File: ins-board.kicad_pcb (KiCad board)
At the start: 2 copper layers, 47 parts, among them P1 CONN_8, P2 PWR, U1 STM32F042C6T6, U2 MIC5201-3.3YS, U3 H3LIS331DL, U4 MPU6000, U5 MS5611-01BA, X1 CRYSTAL 16MHz 10ppm

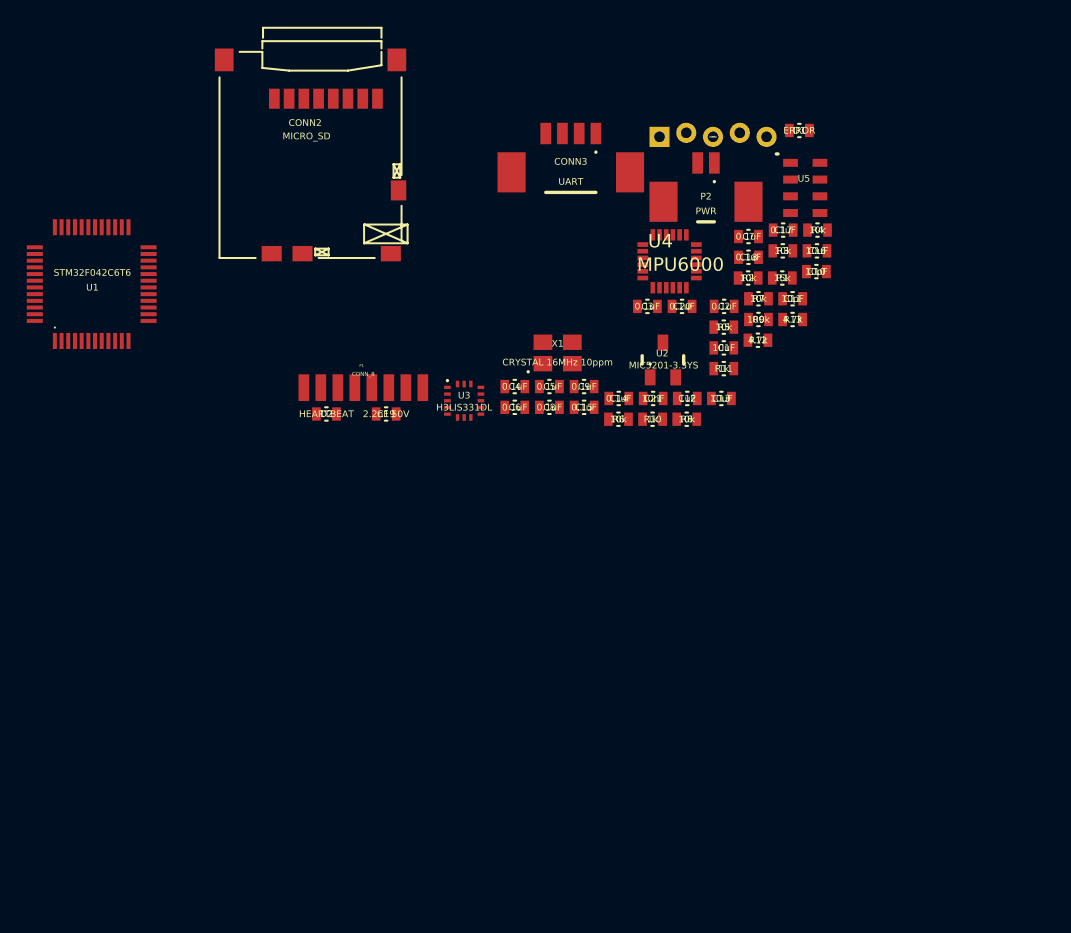
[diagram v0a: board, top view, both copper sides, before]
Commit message: Component placement on PCB
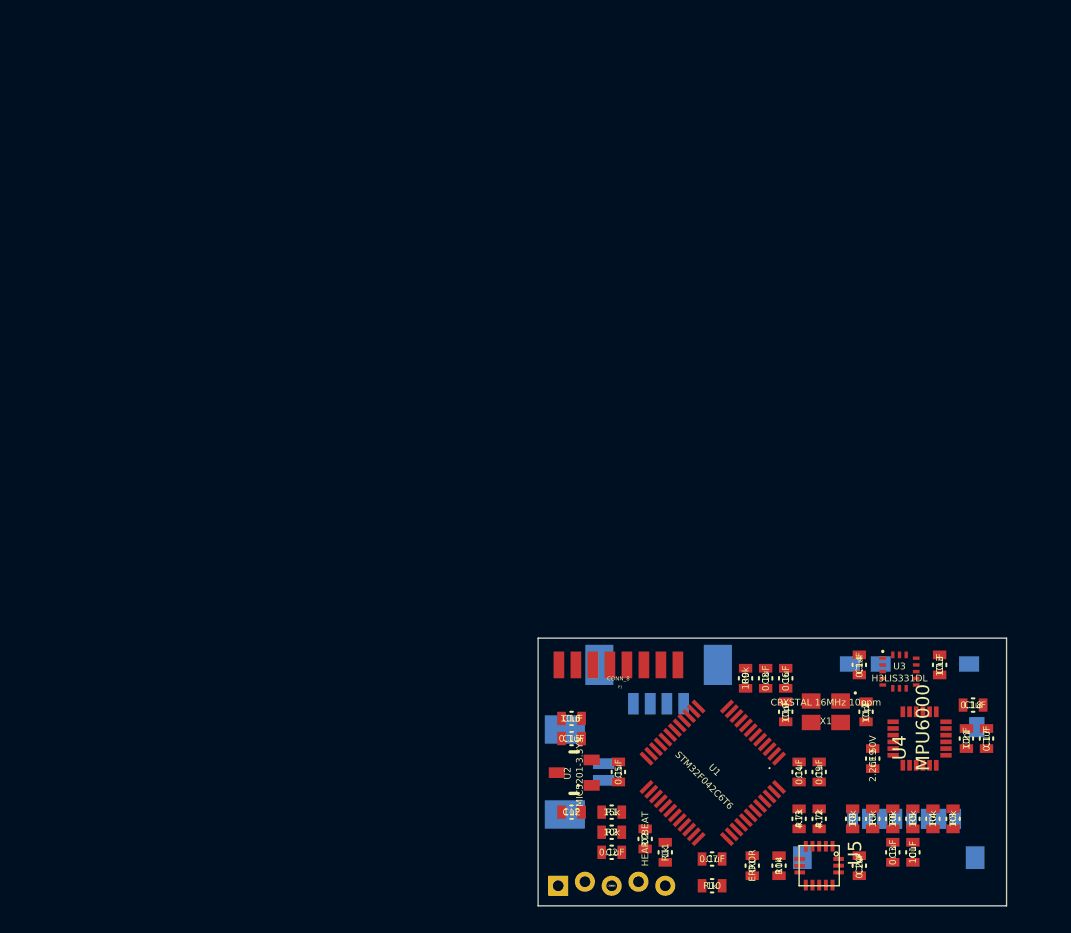
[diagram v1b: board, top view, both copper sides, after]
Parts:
- added R14: 10k, _std:_0603-W, F.Cu at (151.0, 104.5)
- CONN2, CONN3, P2: moved to B.Cu
- U5: value MS5611-01BA -> LPS331AP; footprint _sensors:_MS5611-01BA -> _sensors:_LPS331AP
- moved CONN2 69.0 mm to (156.5, 101.0)
- moved U1 62.5 mm to (151.0, 96.5), turned to 135 degrees
- moved CONN1 56.5 mm to (138.5, 106.0)
- moved D1 55.0 mm to (149.0, 104.5), turned to 270 degrees
- moved U5 49.2 mm to (155.5, 103.0), turned to 270 degrees
- moved C7 46.6 mm to (146.0, 104.0), turned to 180 degrees
- moved R4 44.8 mm to (162.5, 101.0), turned to 90 degrees
- moved C3 44.7 mm to (159.5, 103.5), turned to 270 degrees
- moved C19 44.5 mm to (158.0, 96.5), turned to 90 degrees
- moved R3 44.3 mm to (164.0, 101.0), turned to 90 degrees
- moved P2 43.9 mm to (135.0, 97.5), turned to 90 degrees
- moved C20 43.8 mm to (157.0, 104.5), turned to 270 degrees
- moved R2 42.6 mm to (138.5, 102.0)
- moved R1 41.9 mm to (138.5, 100.5), turned to 180 degrees
- moved C2 41.6 mm to (138.5, 103.5)
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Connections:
- U1 pad 10: (no net) -> Net-(U1-Pad10)
- U1 pad 18: (no net) -> Net-(U1-Pad18)
- U1 pad 2: (no net) -> Net-(U1-Pad2)
- U1 pad 21: (no net) -> Net-(U1-Pad21)
- U1 pad 22: (no net) -> Net-(U1-Pad22)
- U1 pad 3: (no net) -> Net-(U1-Pad3)
- U1 pad 32: (no net) -> Net-(U1-Pad32)
- U1 pad 33: (no net) -> Net-(U1-Pad33)
- U1 pad 4: (no net) -> Net-(U1-Pad4)
- U1 pad 40: (no net) -> Net-(U1-Pad40)
- U1 pad 41: (no net) -> Net-(U1-Pad41)
- U1 pad 45: (no net) -> Net-(U1-Pad45)
- U1 pad 46: (no net) -> Net-(U1-Pad46)
- U3 pad 9: (no net) -> Net-(U3-Pad9)
- U4 pad 22: (no net) -> Net-(U4-Pad22)
- U4 pad 6: (no net) -> Net-(U4-Pad6)
- U4 pad 7: (no net) -> Net-(U4-Pad7)
- U5 pad 2: VCC -> Net-(U5-Pad2)
- U5 pad 3: GND -> Net-(U5-Pad3)
- U5 pad 4: GND -> /INT_I2C_SCL
- U5 pad 6: (no net) -> /INT_I2C_SDA
- U5 pad 7: /INT_I2C_SDA -> GND
- U5 pad 8: /INT_I2C_SCL -> Net-(R14-Pad2)
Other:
- board outline added: 35 x 20 mm

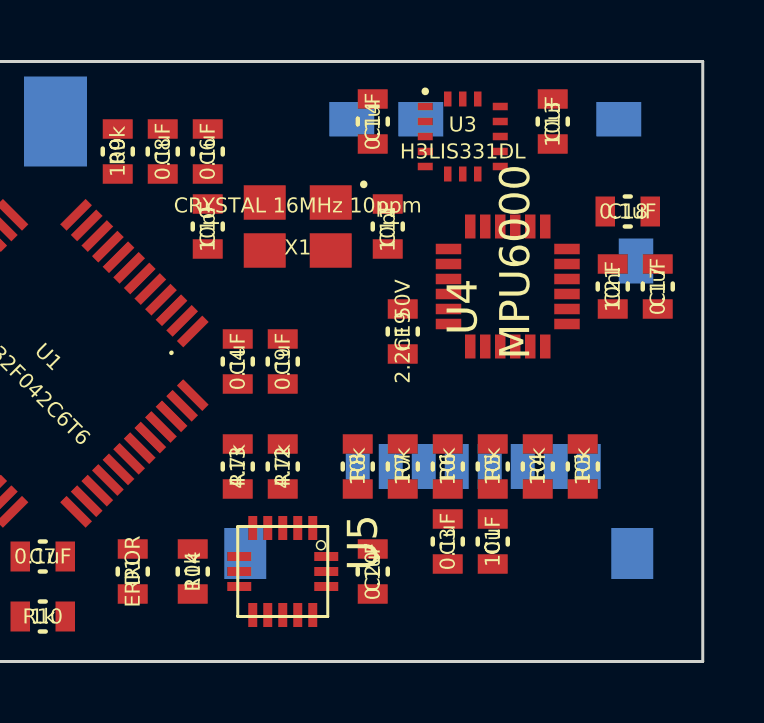
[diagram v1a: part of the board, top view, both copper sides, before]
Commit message: Correct microSD connector footprint & update component placement
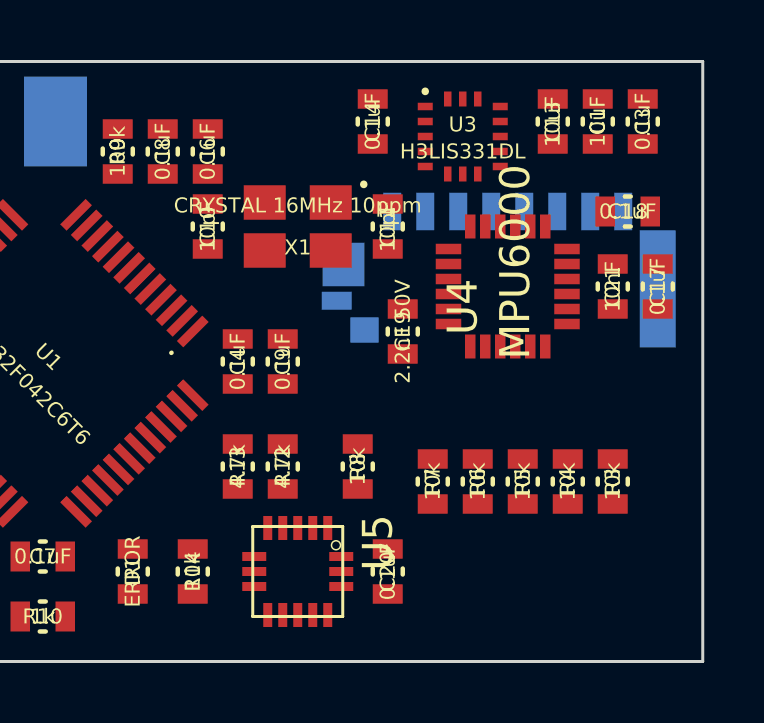
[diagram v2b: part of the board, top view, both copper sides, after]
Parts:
- CONN2: footprint _div:_Molex-microSD-502570-0893 -> _div:_Molex-microSD-WM6701
- moved C3 15.4 mm to (166.0, 89.5)
- moved C1 14.4 mm to (164.5, 89.5)
- moved CONN2 9.86 mm to (161.5, 92.5), turned to 180 degrees
- moved R3 1.12 mm to (165.0, 101.5), turned to 270 degrees
- moved R4 1.12 mm to (163.5, 101.5), turned to 270 degrees
- moved R5 1.12 mm to (162.0, 101.5), turned to 270 degrees
- moved R6 1.12 mm to (160.5, 101.5), turned to 270 degrees
- moved R7 1.12 mm to (159.0, 101.5), turned to 270 degrees
- moved C20 0.50 mm to (157.5, 104.5)
- moved U5 0.50 mm to (156.0, 103.0)

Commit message: update sd-card footprint
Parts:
- moved CONN2 1.10 mm to (161.4, 91.4)
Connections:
- U1 pad 10: Net-(U1-Pad10) -> (no net)
- U1 pad 18: Net-(U1-Pad18) -> (no net)
- U1 pad 2: Net-(U1-Pad2) -> (no net)
- U1 pad 21: Net-(U1-Pad21) -> (no net)
- U1 pad 22: Net-(U1-Pad22) -> (no net)
- U1 pad 3: Net-(U1-Pad3) -> (no net)
- U1 pad 32: Net-(U1-Pad32) -> (no net)
- U1 pad 33: Net-(U1-Pad33) -> (no net)
- U1 pad 4: Net-(U1-Pad4) -> (no net)
- U1 pad 40: Net-(U1-Pad40) -> (no net)
- U1 pad 41: Net-(U1-Pad41) -> (no net)
- U1 pad 45: Net-(U1-Pad45) -> (no net)
- U1 pad 46: Net-(U1-Pad46) -> (no net)
- U3 pad 9: Net-(U3-Pad9) -> (no net)
- U4 pad 22: Net-(U4-Pad22) -> (no net)
- U4 pad 6: Net-(U4-Pad6) -> (no net)
- U4 pad 7: Net-(U4-Pad7) -> (no net)
- U5 pad 11: Net-(U5-Pad11) -> (no net)
- U5 pad 2: Net-(U5-Pad2) -> (no net)
- U5 pad 3: Net-(U5-Pad3) -> (no net)
- U5 pad 9: Net-(U5-Pad9) -> (no net)
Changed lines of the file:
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@@
-(kicad_pcb (version 4) (host pcbnew "(2015-03-28 BZR 5545)-product")
+(kicad_pcb (version 4) (host pcbnew "(2015-03-28 BZR 5547)-product")
   (general
     (links 152)
@@
     (zones 0)
     (modules 48)
-    (nets 57)
+    (nets 36)
   )
   (page A4)
@@
   (net 34 /MPU6000_INT)
   (net 35 "Net-(R14-Pad2)")
-  (net 36 "Net-(U1-Pad2)")
-  (net 37 "Net-(U1-Pad3)")
-  (net 38 "Net-(U1-Pad4)")
-  (net 39 "Net-(U1-Pad10)")
-  (net 40 "Net-(U1-Pad18)")
-  (net 41 "Net-(U1-Pad21)")
-  (net 42 "Net-(U1-Pad22)")
-  (net 43 "Net-(U1-Pad32)")
-  (net 44 "Net-(U1-Pad33)")
-  (net 45 "Net-(U1-Pad40)")
-  (net 46 "Net-(U1-Pad41)")
-  (net 47 "Net-(U1-Pad45)")
-  (net 48 "Net-(U1-Pad46)")
-  (net 49 "Net-(U3-Pad9)")
-  (net 50 "Net-(U4-Pad22)")
-  (net 51 "Net-(U4-Pad7)")
-  (net 52 "Net-(U4-Pad6)")
-  (net 53 "Net-(U5-Pad2)")
-  (net 54 "Net-(U5-Pad3)")
-  (net 55 "Net-(U5-Pad9)")
-  (net 56 "Net-(U5-Pad11)")
   (net_class Default "This is the default net class."
     (clearance 0.2)
@@
     (add_net "Net-(P1-Pad8)")
     (add_net "Net-(R14-Pad2)")
-    (add_net "Net-(U1-Pad10)")
-    (add_net "Net-(U1-Pad18)")
-    (add_net "Net-(U1-Pad2)")
-    (add_net "Net-(U1-Pad21)")
-    (add_net "Net-(U1-Pad22)")
-    (add_net "Net-(U1-Pad3)")
-    (add_net "Net-(U1-Pad32)")
-    (add_net "Net-(U1-Pad33)")
-    (add_net "Net-(U1-Pad4)")
-    (add_net "Net-(U1-Pad40)")
-    (add_net "Net-(U1-Pad41)")
-    (add_net "Net-(U1-Pad45)")
-    (add_net "Net-(U1-Pad46)")
-    (add_net "Net-(U3-Pad9)")
-    (add_net "Net-(U4-Pad22)")
-    (add_net "Net-(U4-Pad6)")
-    (add_net "Net-(U4-Pad7)")
-    (add_net "Net-(U5-Pad11)")
-    (add_net "Net-(U5-Pad2)")
-    (add_net "Net-(U5-Pad3)")
-    (add_net "Net-(U5-Pad9)")
     (add_net VCC)
   )
@@
     (pad 1 smd rect (at 0 0 135) (size 0.3 1.2) (layers F.Cu F.Paste F.Mask)
       (net 2 VCC))
-    (pad 2 smd rect (at 0.5 0 135) (size 0.3 1.2) (layers F.Cu F.Paste F.Mask)
-      (net 36 "Net-(U1-Pad2)"))
-    (pad 3 smd rect (at 1 0 135) (size 0.3 1.2) (layers F.Cu F.Paste F.Mask)
-      (net 37 "Net-(U1-Pad3)"))
-    (pad 4 smd rect (at 1.5 0 135) (size 0.3 1.2) (layers F.Cu F.Paste F.Mask)
-      (net 38 "Net-(U1-Pad4)"))
+    (pad 2 smd rect (at 0.5 0 135) (size 0.3 1.2) (layers F.Cu F.Paste F.Mask))
+    (pad 3 smd rect (at 1 0 135) (size 0.3 1.2) (layers F.Cu F.Paste F.Mask))
+    (pad 4 smd rect (at 1.5 0 135) (size 0.3 1.2) (layers F.Cu F.Paste F.Mask))
     (pad 5 smd rect (at 2 0 135) (size 0.3 1.2) (layers F.Cu F.Paste F.Mask)
       (net 5 "Net-(C10-Pad1)"))
@@
     (pad 9 smd rect (at 4 0 135) (size 0.3 1.2) (layers F.Cu F.Paste F.Mask)
       (net 2 VCC))
-    (pad 10 smd rect (at 4.5 0 135) (size 0.3 1.2) (layers F.Cu F.Paste F.Mask)
-      (net 39 "Net-(U1-Pad10)"))
+    (pad 10 smd rect (at 4.5 0 135) (size 0.3 1.2) (layers F.Cu F.Paste F.Mask))
     (pad 11 smd rect (at 5 0 135) (size 0.3 1.2) (layers F.Cu F.Paste F.Mask)
       (net 3 /V_BAT_MON_AD))
@@
     (pad 17 smd rect (at 7 -3.5 45) (size 0.3 1.2) (layers F.Cu F.Paste F.Mask)
       (net 30 "Net-(P1-Pad8)"))
-    (pad 18 smd rect (at 7 -4 45) (size 0.3 1.2) (layers F.Cu F.Paste F.Mask)
-      (net 40 "Net-(U1-Pad18)"))
+    (pad 18 smd rect (at 7 -4 45) (size 0.3 1.2) (layers F.Cu F.Paste F.Mask))
     (pad 19 smd rect (at 7 -4.5 45) (size 0.3 1.2) (layers F.Cu F.Paste F.Mask)
       (net 33 /H3LIS331DL_INT1))
     (pad 20 smd rect (at 7 -5 45) (size 0.3 1.2) (layers F.Cu F.Paste F.Mask)
       (net 34 /MPU6000_INT))
-    (pad 21 smd rect (at 7 -5.5 45) (size 0.3 1.2) (layers F.Cu F.Paste F.Mask)
-      (net 41 "Net-(U1-Pad21)"))
-    (pad 22 smd rect (at 7 -6 45) (size 0.3 1.2) (layers F.Cu F.Paste F.Mask)
-      (net 42 "Net-(U1-Pad22)"))
+    (pad 21 smd rect (at 7 -5.5 45) (size 0.3 1.2) (layers F.Cu F.Paste F.Mask))
+    (pad 22 smd rect (at 7 -6 45) (size 0.3 1.2) (layers F.Cu F.Paste F.Mask))
     (pad 23 smd rect (at 7 -6.5 45) (size 0.3 1.2) (layers F.Cu F.Paste F.Mask)
       (net 1 GND))
@@
     (pad 31 smd rect (at 2.5 -8.5 315) (size 0.3 1.2) (layers F.Cu F.Paste F.Mask)
       (net 20 /UART_RX))
-    (pad 32 smd rect (at 2 -8.5 315) (size 0.3 1.2) (layers F.Cu F.Paste F.Mask)
-      (net 43 "Net-(U1-Pad32)"))
-    (pad 33 smd rect (at 1.5 -8.5 315) (size 0.3 1.2) (layers F.Cu F.Paste F.Mask)
-      (net 44 "Net-(U1-Pad33)"))
+    (pad 32 smd rect (at 2 -8.5 315) (size 0.3 1.2) (layers F.Cu F.Paste F.Mask))
+    (pad 33 smd rect (at 1.5 -8.5 315) (size 0.3 1.2) (layers F.Cu F.Paste F.Mask))
     (pad 34 smd rect (at 1 -8.5 315) (size 0.3 1.2) (layers F.Cu F.Paste F.Mask)
       (net 11 /STM32F4_SWDIO))
@@
     (pad 39 smd rect (at -1.5 -6 225) (size 0.3 1.2) (layers F.Cu F.Paste F.Mask)
       (net 18 /SD_DETECT))
-    (pad 40 smd rect (at -1.5 -5.5 225) (size 0.3 1.2) (layers F.Cu F.Paste F.Mask)
-      (net 45 "Net-(U1-Pad40)"))
-    (pad 41 smd rect (at -1.5 -5 225) (size 0.3 1.2) (layers F.Cu F.Paste F.Mask)
-      (net 46 "Net-(U1-Pad41)"))
+    (pad 40 smd rect (at -1.5 -5.5 225) (size 0.3 1.2) (layers F.Cu F.Paste F.Mask))
+    (pad 41 smd rect (at -1.5 -5 225) (size 0.3 1.2) (layers F.Cu F.Paste F.Mask))
     (pad 42 smd rect (at -1.5 -4.5 225) (size 0.3 1.2) (layers F.Cu F.Paste F.Mask)
       (net 31 /INT_I2C_SCL))
@@
     (pad 44 smd rect (at -1.5 -3.5 225) (size 0.3 1.2) (layers F.Cu F.Paste F.Mask)
       (net 1 GND))
-    (pad 45 smd rect (at -1.5 -3 225) (size 0.3 1.2) (layers F.Cu F.Paste F.Mask)
-      (net 47 "Net-(U1-Pad45)"))
-    (pad 46 smd rect (at -1.5 -2.5 225) (size 0.3 1.2) (layers F.Cu F.Paste F.Mask)
-      (net 48 "Net-(U1-Pad46)"))
+    (pad 45 smd rect (at -1.5 -3 225) (size 0.3 1.2) (layers F.Cu F.Paste F.Mask))
+    (pad 46 smd rect (at -1.5 -2.5 225) (size 0.3 1.2) (layers F.Cu F.Paste F.Mask))
     (pad 47 smd rect (at -1.5 -2 225) (size 0.3 1.2) (layers F.Cu F.Paste F.Mask)
       (net 1 GND))
@@
     (pad 11 smd rect (at 1.25 0) (size 0.5 0.25) (layers F.Cu F.Paste F.Mask)
       (net 33 /H3LIS331DL_INT1))
-    (pad 9 smd rect (at 1.25 1) (size 0.5 0.25) (layers F.Cu F.Paste F.Mask)
-      (net 49 "Net-(U3-Pad9)"))
+    (pad 9 smd rect (at 1.25 1) (size 0.5 0.25) (layers F.Cu F.Paste F.Mask))
     (pad 10 smd rect (at 1.25 0.5) (size 0.5 0.25) (layers F.Cu F.Paste F.Mask)
       (net 1 GND))
@@
     (pad 23 smd rect (at -0.75 -1.975 180) (size 0.85 0.35) (layers F.Cu F.Mask)
       (net 31 /INT_I2C_SCL))
-    (pad 22 smd rect (at -0.25 -1.975 180) (size 0.85 0.35) (layers F.Cu F.Mask)
-      (net 50 "Net-(U4-Pad22)"))
+    (pad 22 smd rect (at -0.25 -1.975 180) (size 0.85 0.35) (layers F.Cu F.Mask))
     (pad 21 smd rect (at 0.25 -1.975 180) (size 0.85 0.35) (layers F.Cu F.Mask))
     (pad 20 smd rect (at 0.75 -1.975 180) (size 0.85 0.35) (layers F.Cu F.Mask)
@@
     (pad 8 smd rect (at -0.75 1.975 180) (size 0.85 0.35) (layers F.Cu F.Mask)
       (net 2 VCC))
-    (pad 7 smd rect (at -1.25 1.975 180) (size 0.85 0.35) (layers F.Cu F.Mask)
-      (net 51 "Net-(U4-Pad7)"))
+    (pad 7 smd rect (at -1.25 1.975 180) (size 0.85 0.35) (layers F.Cu F.Mask))
     (pad 16 smd rect (at 2 -0.25 90) (size 0.8 0.35) (layers F.Cu F.Mask))
     (pad 15 smd rect (at 2 0.25 90) (size 0.8 0.35) (layers F.Cu F.Mask))
@@
     (pad 13 smd rect (at 2 1.25 90) (size 0.8 0.35) (layers F.Cu F.Mask)
       (net 2 VCC))
-    (pad 6 smd rect (at -2 1.25 90) (size 0.8 0.35) (layers F.Cu F.Mask)
-      (net 52 "Net-(U4-Pad6)"))
+    (pad 6 smd rect (at -2 1.25 90) (size 0.8 0.35) (layers F.Cu F.Mask))
     (pad 5 smd rect (at -2 0.75 90) (size 0.8 0.35) (layers F.Cu F.Mask))
     (pad 1 smd rect (at -2 -1.25 90) (size 0.8 0.35) (layers F.Cu F.Mask)
@@
     (pad 1 smd rect (at 0.05 0.5 270) (size 0.8 0.3) (layers F.Cu F.Paste F.Mask)
       (net 2 VCC))
-    (pad 2 smd rect (at 0.05 1 270) (size 0.8 0.3) (layers F.Cu F.Paste F.Mask)
-      (net 53 "Net-(U5-Pad2)"))
-    (pad 3 smd rect (at 0.05 1.5 270) (size 0.8 0.3) (layers F.Cu F.Paste F.Mask)
-      (net 54 "Net-(U5-Pad3)"))
+    (pad 2 smd rect (at 0.05 1 270) (size 0.8 0.3) (layers F.Cu F.Paste F.Mask))
+    (pad 3 smd rect (at 0.05 1.5 270) (size 0.8 0.3) (layers F.Cu F.Paste F.Mask))
     (pad 4 smd rect (at 0.05 2 270) (size 0.8 0.3) (layers F.Cu F.Paste F.Mask)
       (net 31 /INT_I2C_SCL))
     (pad 5 smd rect (at 0.05 2.5 270) (size 0.8 0.3) (layers F.Cu F.Paste F.Mask)
       (net 1 GND))
-    (pad 9 smd rect (at 2.95 2.5 270) (size 0.8 0.3) (layers F.Cu F.Paste F.Mask)
-      (net 55 "Net-(U5-Pad9)"))
+    (pad 9 smd rect (at 2.95 2.5 270) (size 0.8 0.3) (layers F.Cu F.Paste F.Mask))
     (pad 10 smd rect (at 2.95 2 270) (size 0.8 0.3) (layers F.Cu F.Paste F.Mask)
       (net 1 GND))
-    (pad 11 smd rect (at 2.95 1.5 270) (size 0.8 0.3) (layers F.Cu F.Paste F.Mask)
-      (net 56 "Net-(U5-Pad11)"))
+    (pad 11 smd rect (at 2.95 1.5 270) (size 0.8 0.3) (layers F.Cu F.Paste F.Mask))
     (pad 12 smd rect (at 2.95 1 270) (size 0.8 0.3) (layers F.Cu F.Paste F.Mask)
       (net 1 GND))
@@
   )
   (module _div:_Molex-microSD-WM6701 (layer B.Cu)
-    (at 161.5 92.5 180)
-    (fp_text reference CONN2 (at 0 -3.5 360) (layer B.SilkS)
+    (at 161.4 91.4 180)
+    (fp_text reference CONN2 (at 0 2 360) (layer B.SilkS)
       (effects (font (size 0.5 0.5) (thickness 0.1)) (justify mirror))
     )
-    (fp_text value MICRO_SD (at 0 -2.5 360) (layer B.SilkS)
+    (fp_text value MICRO_SD (at 0 3 360) (layer B.SilkS)
       (effects (font (size 0.5 0.5) (thickness 0.1)) (justify mirror))
     )
@@
     (pad 1 smd rect (at 3.85 0) (size 0.6 1.25) (layers B.Cu B.Paste B.Mask)
       (net 17 "Net-(CONN2-Pad1)"))
-    (pad SHD smd rect (at 5.475 -1.765) (size 1.4 1.45) (layers B.Cu B.Paste B.Mask)
+    (pad SHD smd rect (at 5.475 -1.765) (size 1.45 1.45) (layers B.Cu B.Paste B.Mask)
       (net 1 GND))
     (pad 10 smd rect (at 5.7 -2.975) (size 1 0.6) (layers B.Cu B.Paste B.Mask)
